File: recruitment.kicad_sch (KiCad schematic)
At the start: 1 part

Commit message: Aggiornamento Appunti
Duh
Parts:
- added K1: Relay_SPST_Latching_2coil, symbol Relay:Relay_SPST_Latching_2coil
- added R1: R, symbol Device:R_US
- added U1: XL1509-12, Package_SO:SOIC-8_3.9x4.9mm_P1.27mm, symbol Regulator_Switching:XL1509-12
- C1: value 1F -> C; footprint Capacitor_SMD:C_0805_2012Metric -> (none)
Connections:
- net at C1.1: no longer C1.2
- new net GND: K1.A2, K1.B1, U1.4 (~{EN}), U1.5 (GND), U1.6 (GND), U1.7 (GND), U1.8 (GND)
- new net Monitor Supply: U1.1 (VIN)

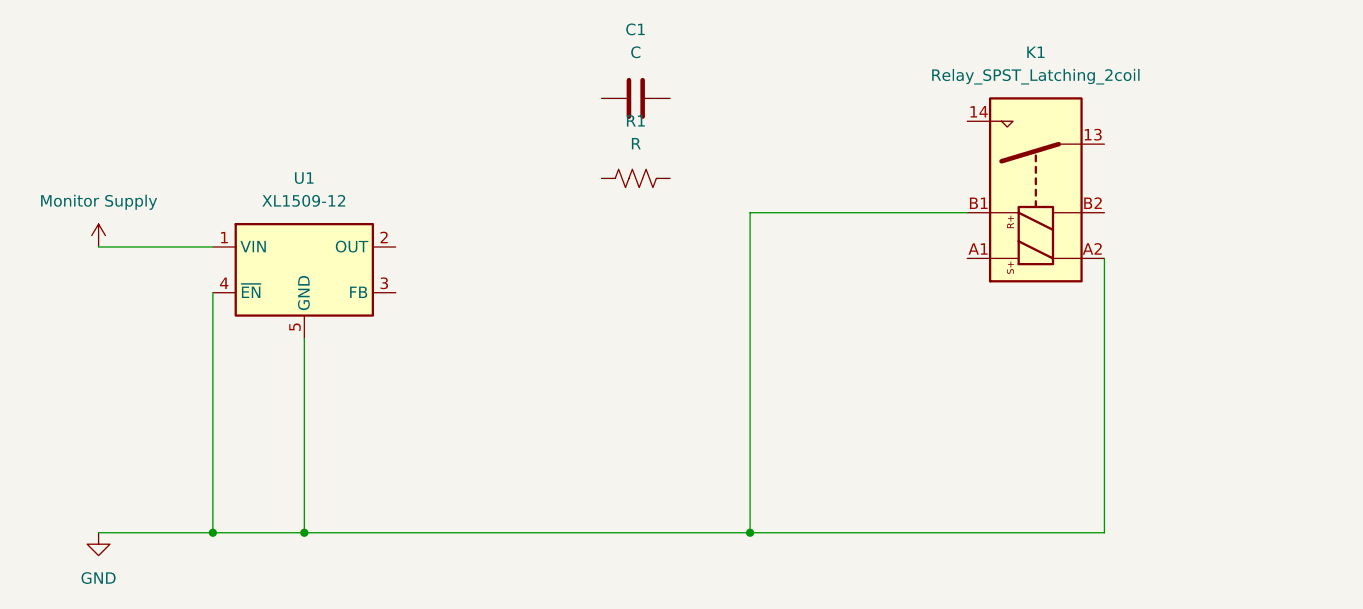
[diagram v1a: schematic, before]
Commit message: Circuit Update
Uploaded circuit with Hierarchical designs (Label + Sub-Circuits)
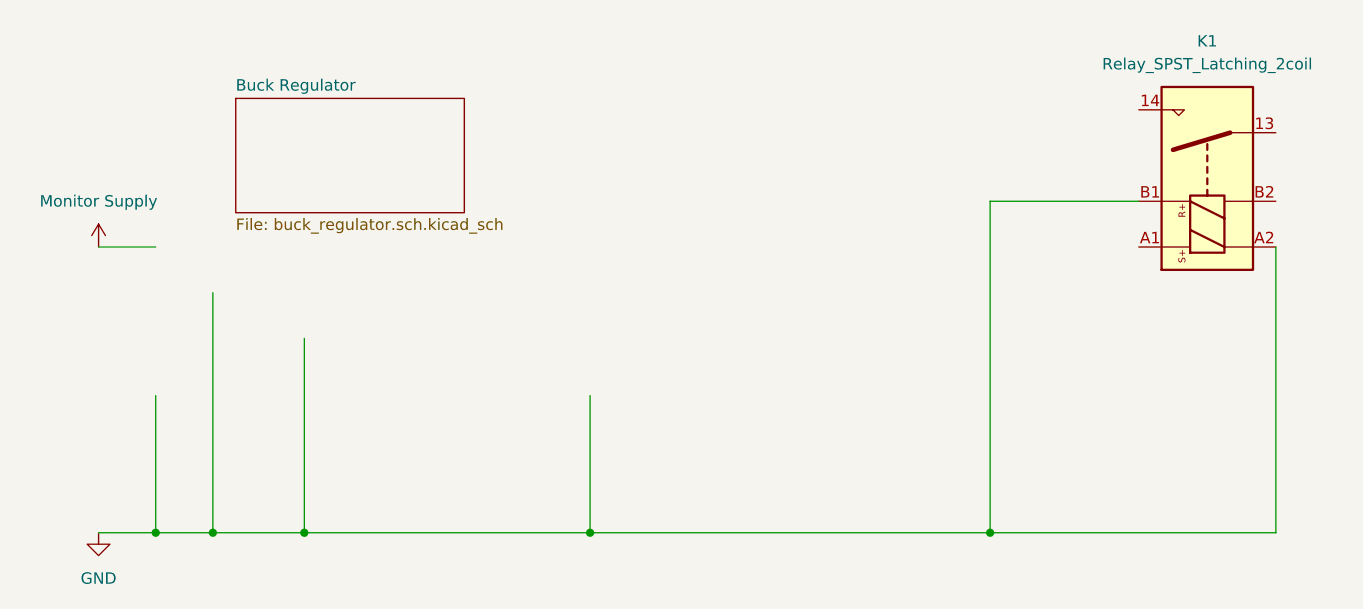
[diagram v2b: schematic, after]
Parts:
- removed C1: C, symbol Device:C
- removed R1: R, symbol Device:R_US
- removed U1: XL1509-12, Package_SO:SOIC-8_3.9x4.9mm_P1.27mm, symbol Regulator_Switching:XL1509-12
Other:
- added sheet Buck Regulator (buck_regulator.sch.kicad_sch)
- moved on the sheet: K1

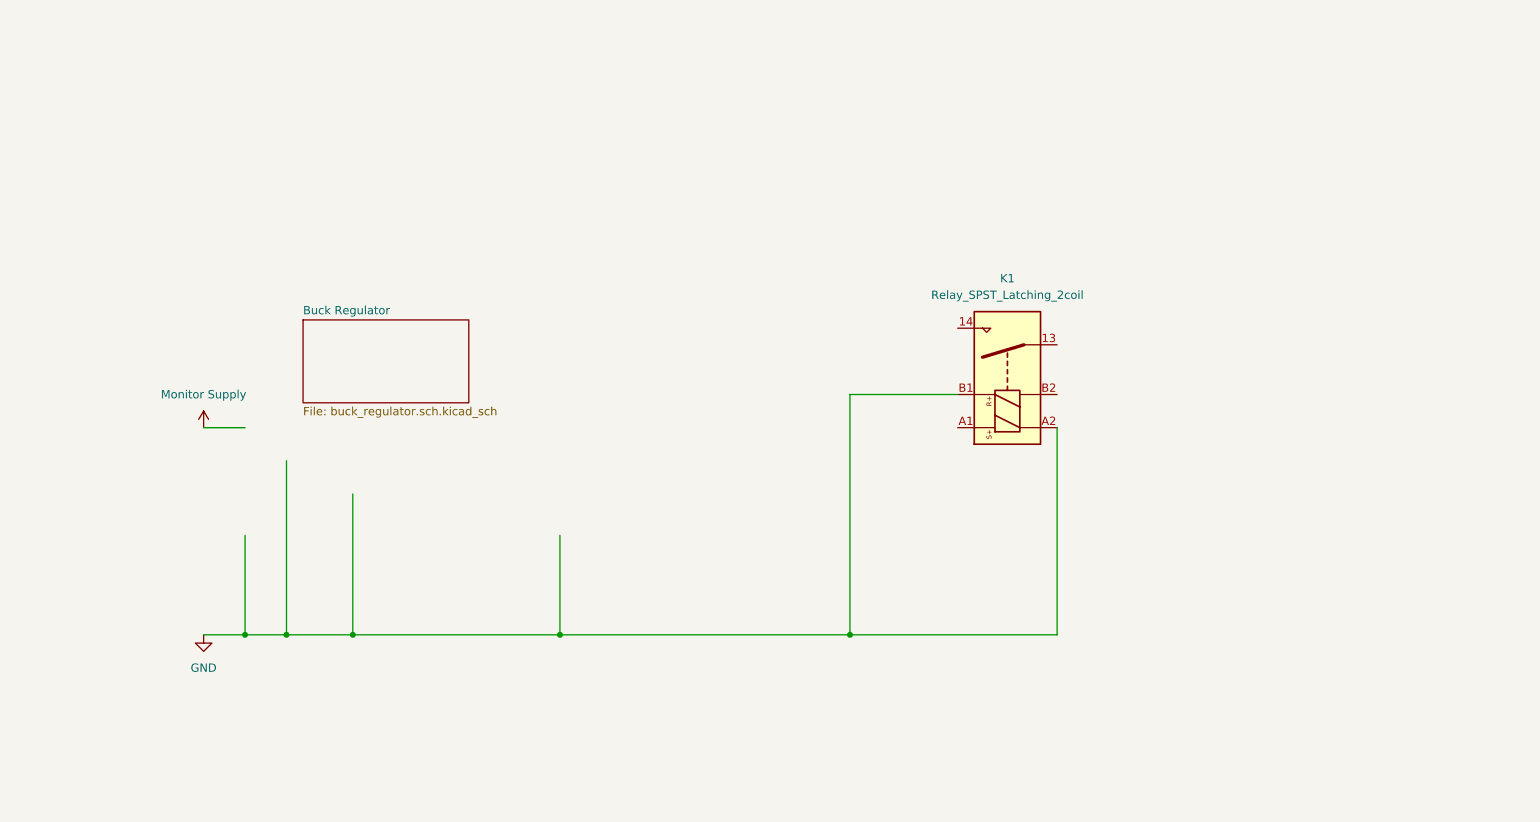
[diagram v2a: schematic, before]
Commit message: Update Hall Sensor
Swapped Bilateral for Unilateral hall sensor and added Hierarchy. Added Load tags
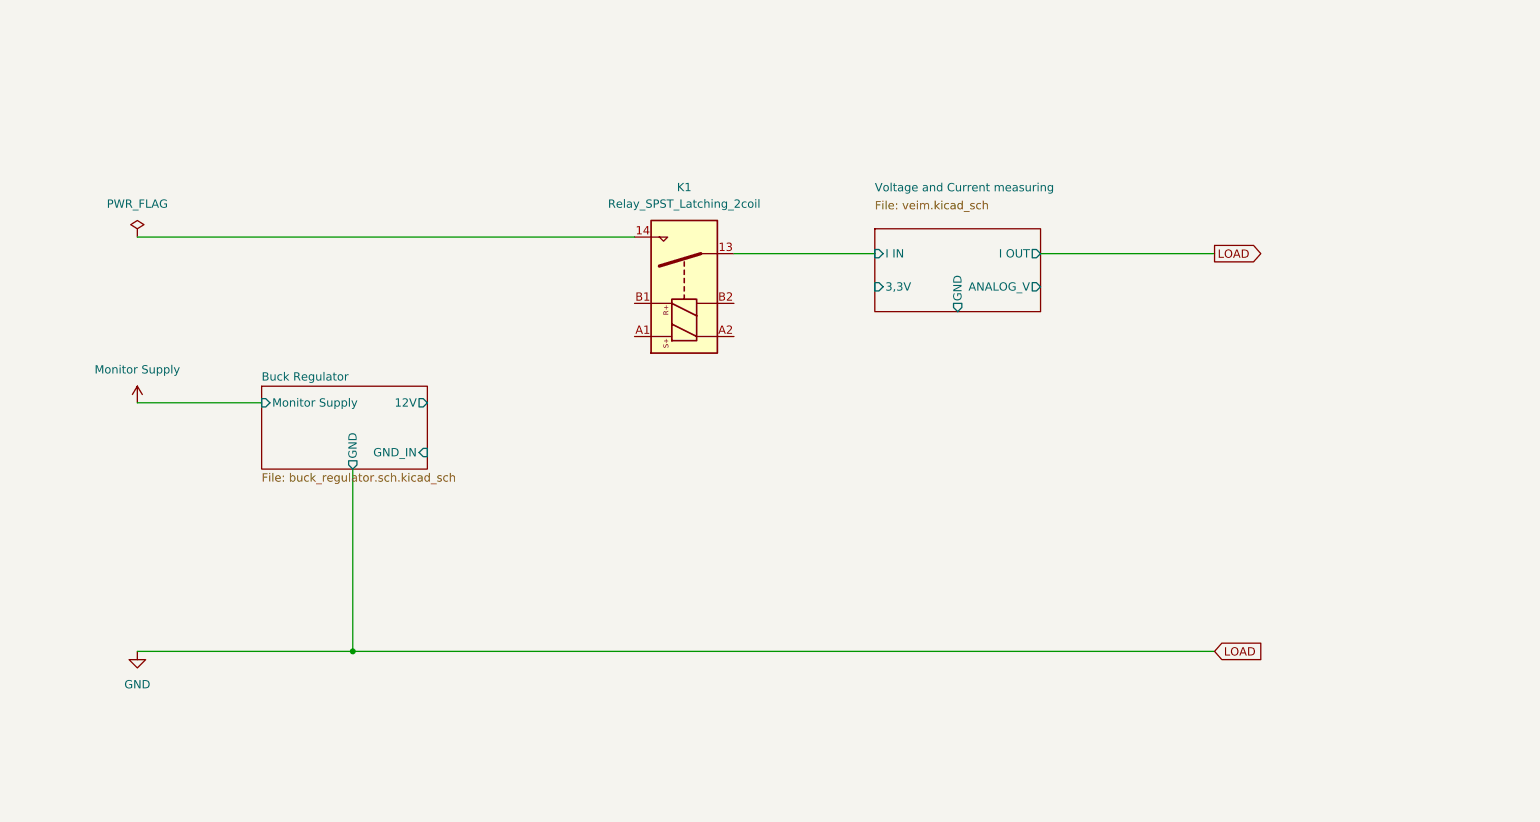
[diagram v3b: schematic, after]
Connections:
- net GND: no longer K1.A2, K1.B1
- net Voltage and Current measuring/I IN: now reaches K1.13
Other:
- added sheet Voltage and Current measuring (veim.kicad_sch)
- sheet Buck Regulator ports: added 12V, GND, GND_IN, Monitor Supply; removed none
- moved on the sheet: K1

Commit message: Big? Update
Turned back to Bilateral Hall Sensor, added Analog Voltage Multiplier.
Added 555 oneshot timer for closing relay on boot.
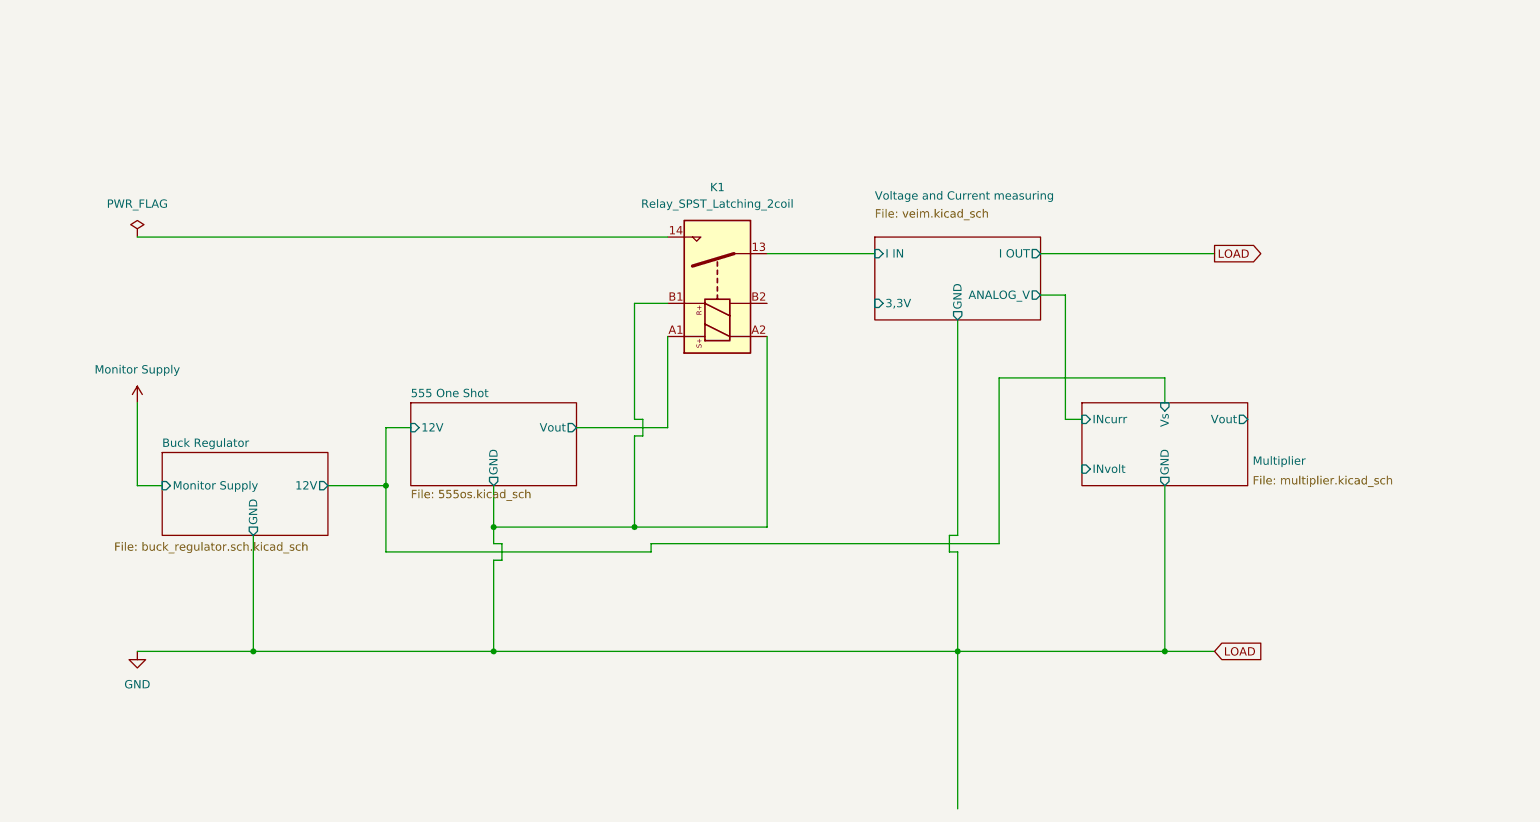
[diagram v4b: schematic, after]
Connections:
- net GND: now also K1.A2, K1.B1
- net 555 One Shot/Vout: now reaches K1.A1
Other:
- added sheet 555 One Shot (555os.kicad_sch)
- added sheet Multiplier (multiplier.kicad_sch)
- sheet Buck Regulator ports: added none; removed GND_IN
- moved on the sheet: K1

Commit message: Safety update
Updating not to loose work
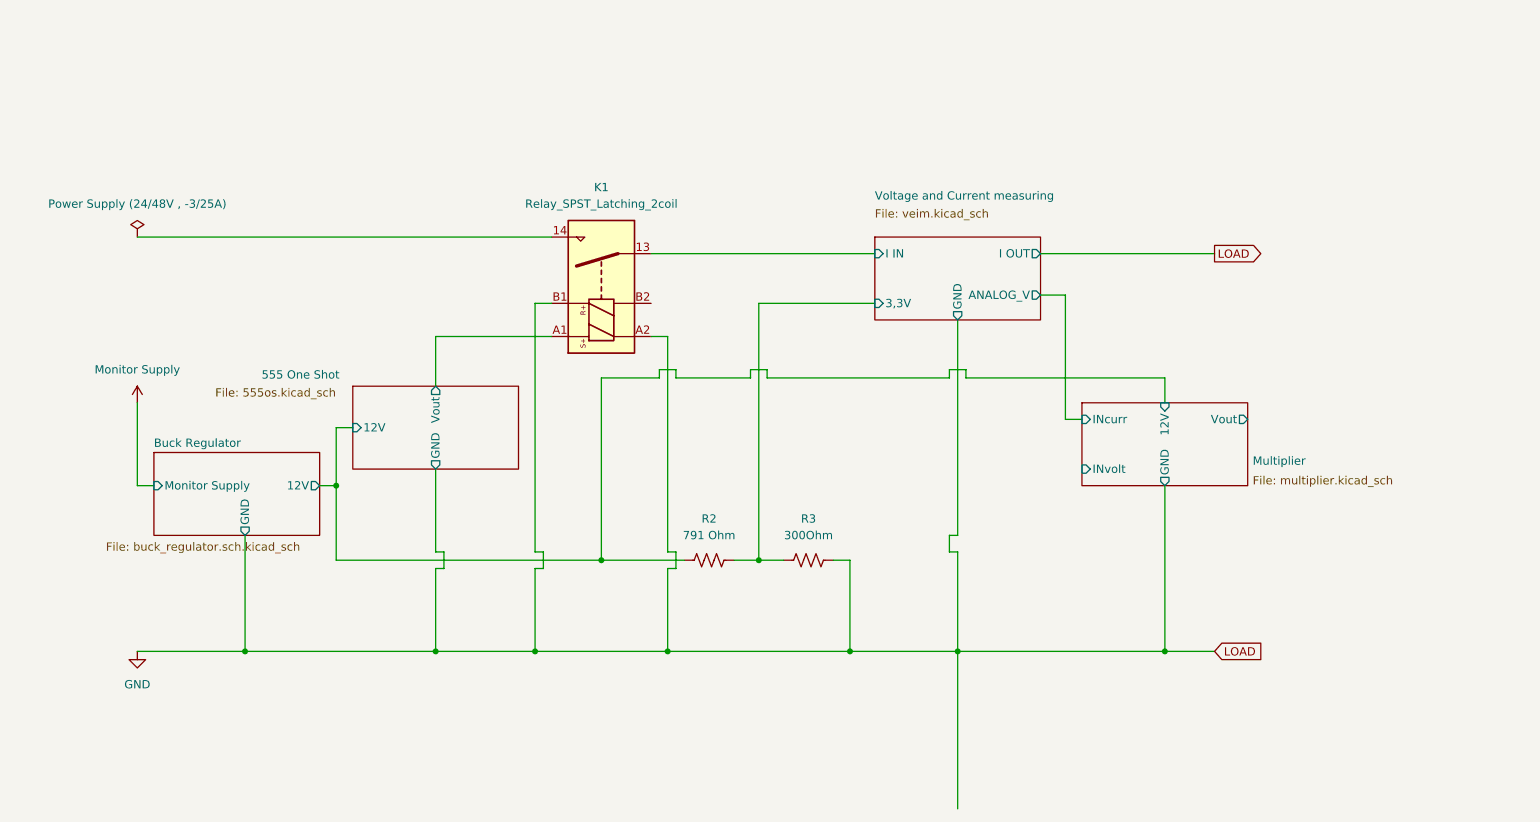
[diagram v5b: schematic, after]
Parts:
- added R2: 791 Ohm, symbol Device:R_US
- added R3: 300Ohm, symbol Device:R_US
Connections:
- net 555 One Shot/12V: now also R2.1
- net GND: now also R3.2
- net Voltage and Current measuring/3,3V: now also R2.2, R3.1
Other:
- sheet Multiplier ports: added 12V; removed Vs
- moved on the sheet: K1

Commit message: Ri-organization
Put circuit in better order
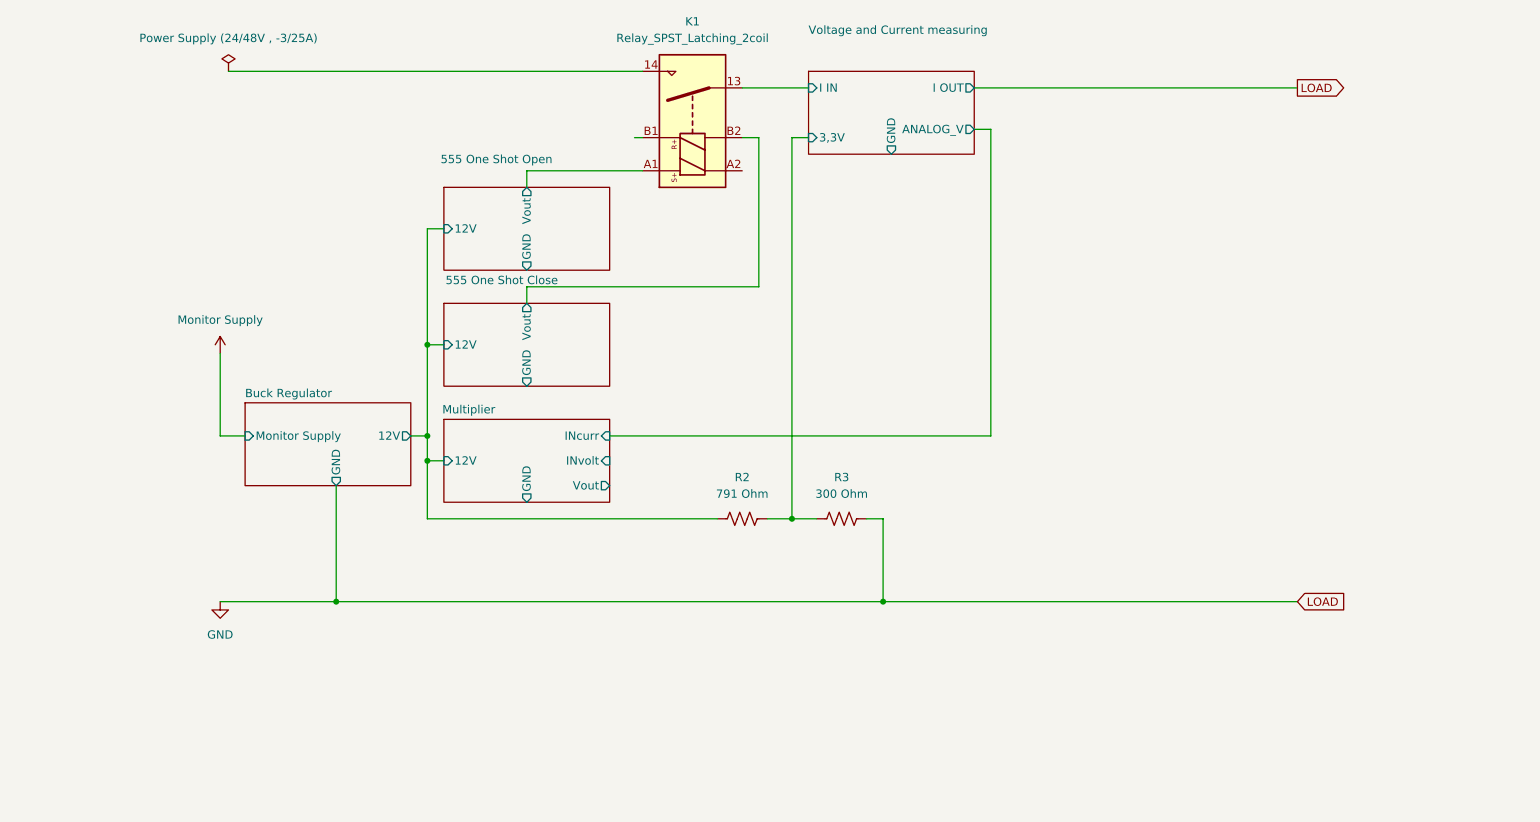
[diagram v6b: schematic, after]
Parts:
- R3: value 300Ohm -> 300 Ohm
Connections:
- net GND: no longer K1.A2, K1.B1
- net 555 One Shot Close/Vout: now reaches K1.B2
- net 555 One Shot Open/12V renamed 555 One Shot Close/12V
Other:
- sheet 555 One Shot renamed 555 One Shot Open
- added sheet 555 One Shot Close (555os.kicad_sch)
- moved on the sheet: K1, R2, R3
